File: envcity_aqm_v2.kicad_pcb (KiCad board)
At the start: 2 copper layers, 100 x 100 mm, 133 parts, among them IC1 DS1307ZN+, IC2 DMMT5401-7F, IC3 DMMT5401-7F, IC4 DMMT5401-7-F, IC6 ESP32-S2-SOLO-N4R2, J1 USB_B_Micro, J12 Conn_01x06_Male, J13 Conn_01x06_Male, J14 Conn_01x08_Pin, J15 Conn_01x02_Male, J16 Conn_01x02_Male, J2 Screw_Terminal_01x02, J3 Screw_Terminal_01x02, J4 Micro_SD_Card, J5 Conn_01x03_Male, J6 Conn_01x04_Male, J7 Conn_01x06_Pin, Q1 DMG2301L / DMP2045U, Q2 DMG2301L / DMP2045U, Q3 DMG2301L, Q4 DMG2301L, Q5 DMG2301L / DMP2045U, Q6 DMG2301L, Q7 DMN10H220L, Q8 DMN10H220L, SW1 RESET, SW2 BOOT, U1 TP4056, U10 RFM95W-915S2, U11 ADS1115IDGS, U2 USBLC6-2SC6, U3 MT3608, U4 MT3608, U5 LM2596S-5, U6 AP2112K-3.3, U7 DHT11, U8 AP2112K-3.3, U9 74HC4067DB, Y2 AB26TRB

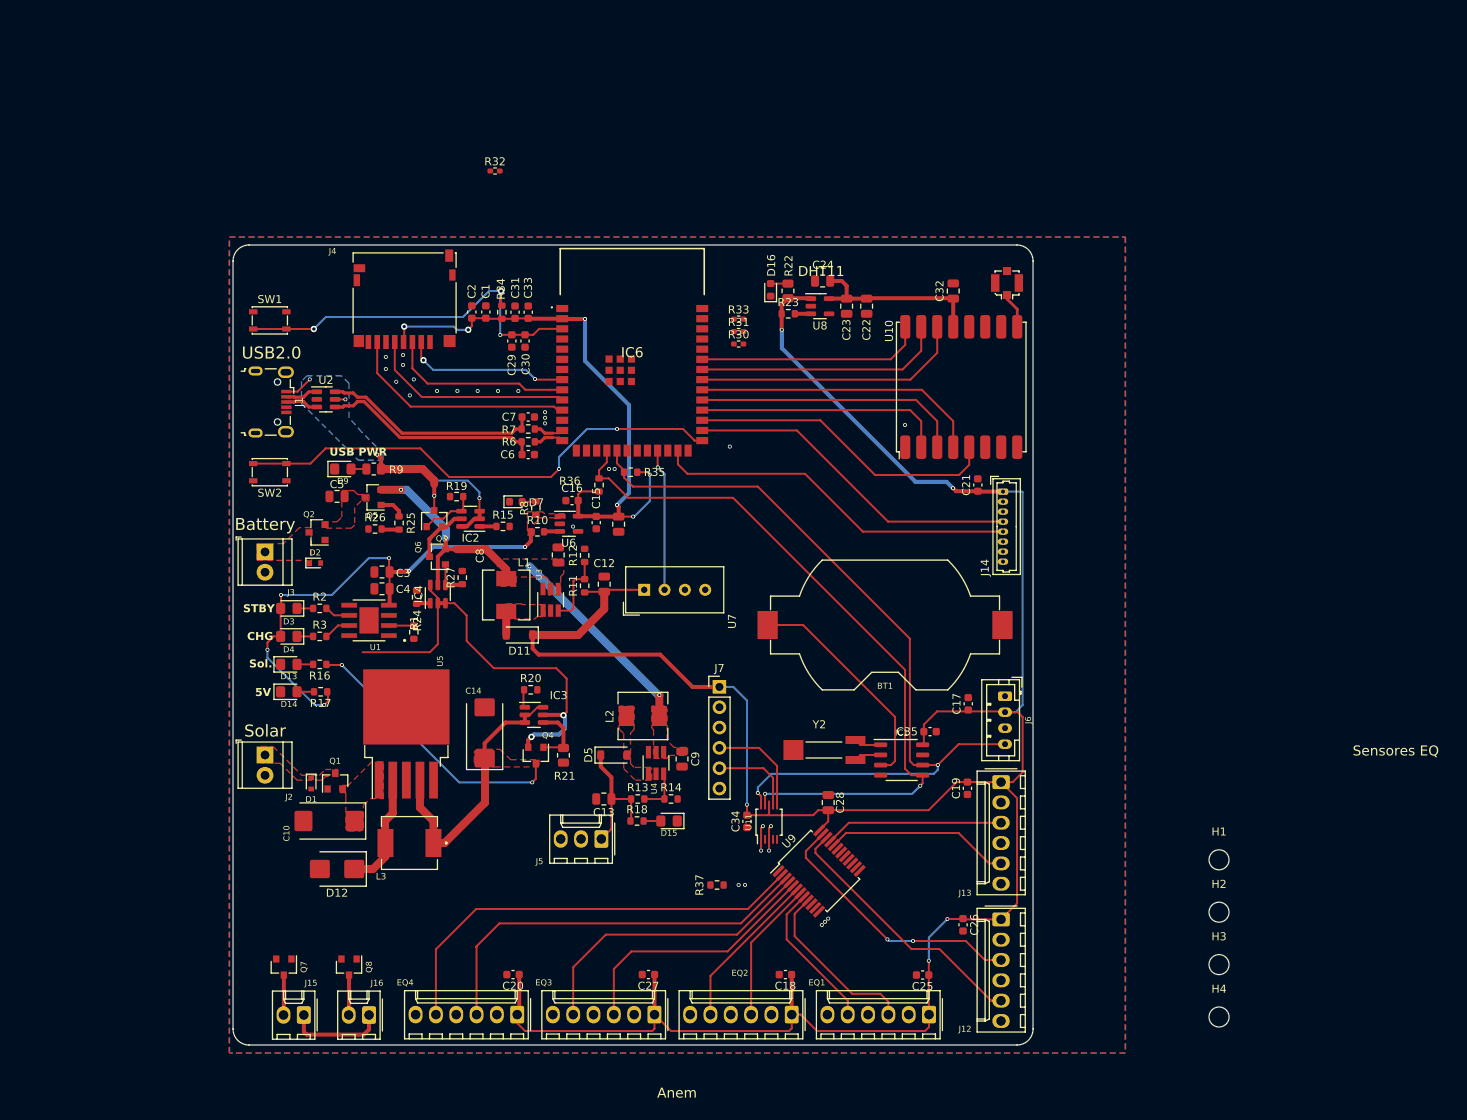
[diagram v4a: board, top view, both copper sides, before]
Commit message: Trocando o modelo do cartaoSD
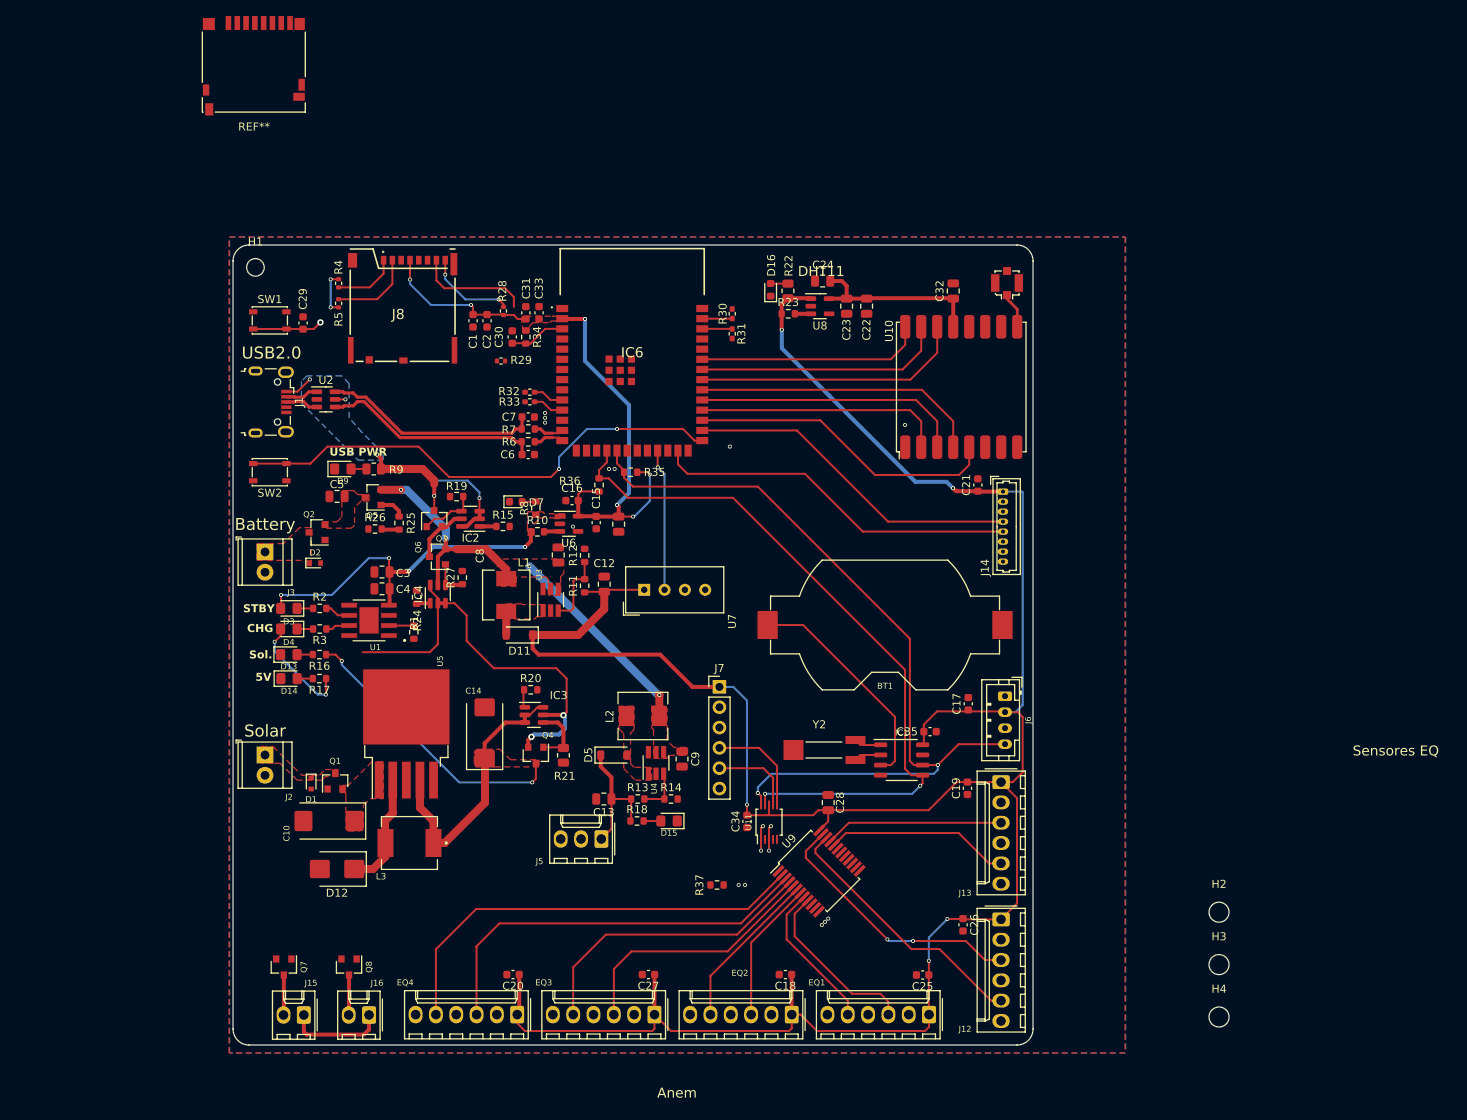
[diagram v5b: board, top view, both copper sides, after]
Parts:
- removed J4: Micro_SD_Card, Connector_Card:microSD_HC_Hirose_DM3D-SF
- added J8: 503398-1892, Molex 503398-1892:503398-1892, F.Cu at (125.7, 60.5)
- added R28: 10k, Resistor_SMD:R_0402_1005Metric, F.Cu at (144.8, 68.2)
- added R29: 10k, Resistor_SMD:R_0402_1005Metric, F.Cu at (144.5, 74.5)
- added R4: 10k, Resistor_SMD:R_0402_1005Metric, F.Cu at (124.2, 64.8)
- added R5: 10k, Resistor_SMD:R_0402_1005Metric, F.Cu at (124.2, 67.3)
- added REF**: microSD_HC_Hirose_DM3D-SF, Connector_Card:microSD_HC_Hirose_DM3D-SF, F.Cu at (113.6, 37.6)
- H1: footprint MountingHole:MountingHole_2.5mm -> MountingHole:MountingHole_2.2mm_M2
- moved H1 141.4 mm to (113.8, 62.8)
- moved R33 28.1 mm to (148.1, 79.6), turned to 180 degrees
- moved R32 28.0 mm to (148.1, 78.4), turned to 180 degrees
- moved C29 26.2 mm to (119.8, 69.8), turned to 90 degrees
- moved R34 4.31 mm to (147.6, 71.5), turned to -90 degrees
- moved R30 3.86 mm to (173.4, 68.6), turned to 90 degrees
- moved C2 2.20 mm to (142.8, 69.5), turned to -90 degrees
- moved C1 1.94 mm to (141.0, 69.5), turned to -90 degrees
- moved C30 1.68 mm to (145.9, 71.5), turned to 90 degrees
- moved R17 1.66 mm to (121.8, 114.2)
- moved D14 1.65 mm to (118.0, 114.2)
- moved C31 1.35 mm to (147.6, 68.5)
- moved C33 1.35 mm to (149.2, 68.5)
- moved R16 1.23 mm to (121.8, 111.2)
- moved D13 1.22 mm to (118.0, 111.2)
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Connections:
- IC6 pad 10: /SD_SCK -> /S2
- IC6 pad 11: /SD_MISO -> /S3
- IC6 pad 38: /IO2 -> /S1
- IC6 pad 39: /IO1 -> /S0
- IC6 pad 4: /S0 -> unconnected-(IC6-IO4-Pad4)
- IC6 pad 5: /S1 -> /SD_CS
- IC6 pad 6: /S2 -> /SD_MOSI
- IC6 pad 7: /S3 -> /SD_SCK
- IC6 pad 8: /SD_CS -> /SD_MISO
- IC6 pad 9: /SD_MOSI -> unconnected-(IC6-IO16-Pad9)
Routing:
- net /EN: track 48.4 -> 15.8 mm, vias 3 -> 1
- net /SD_SCK: track 26.0 -> 0.00 mm
- net /SD_MOSI: track 23.1 -> 0.07 mm
- net /SD_MISO: track 28.9 -> 14.3 mm
- net /DAT1: track 0.00 -> 11.3 mm, vias 0 -> 2
- net /SD_CS: track 20.7 -> 10.5 mm, vias 2 -> 0
- net /DAT2: track 0.00 -> 8.01 mm
- net +5V: track 395.0 -> 390.0 mm
- net /S3: track 0.00 -> 3.88 mm
- net /S2: track 0.00 -> 3.85 mm
- net /S1: track 0.00 -> 3.76 mm
- net /S0: track 0.00 -> 3.76 mm
- net +3V3: track 73.9 -> 76.2 mm, vias 6 -> 8
- net Vsolar_reg: track 68.9 -> 69.5 mm
- net GND: vias 29 -> 17
- added copper zone on F.Cu, net +3V3

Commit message: running DRC and fixing some errors
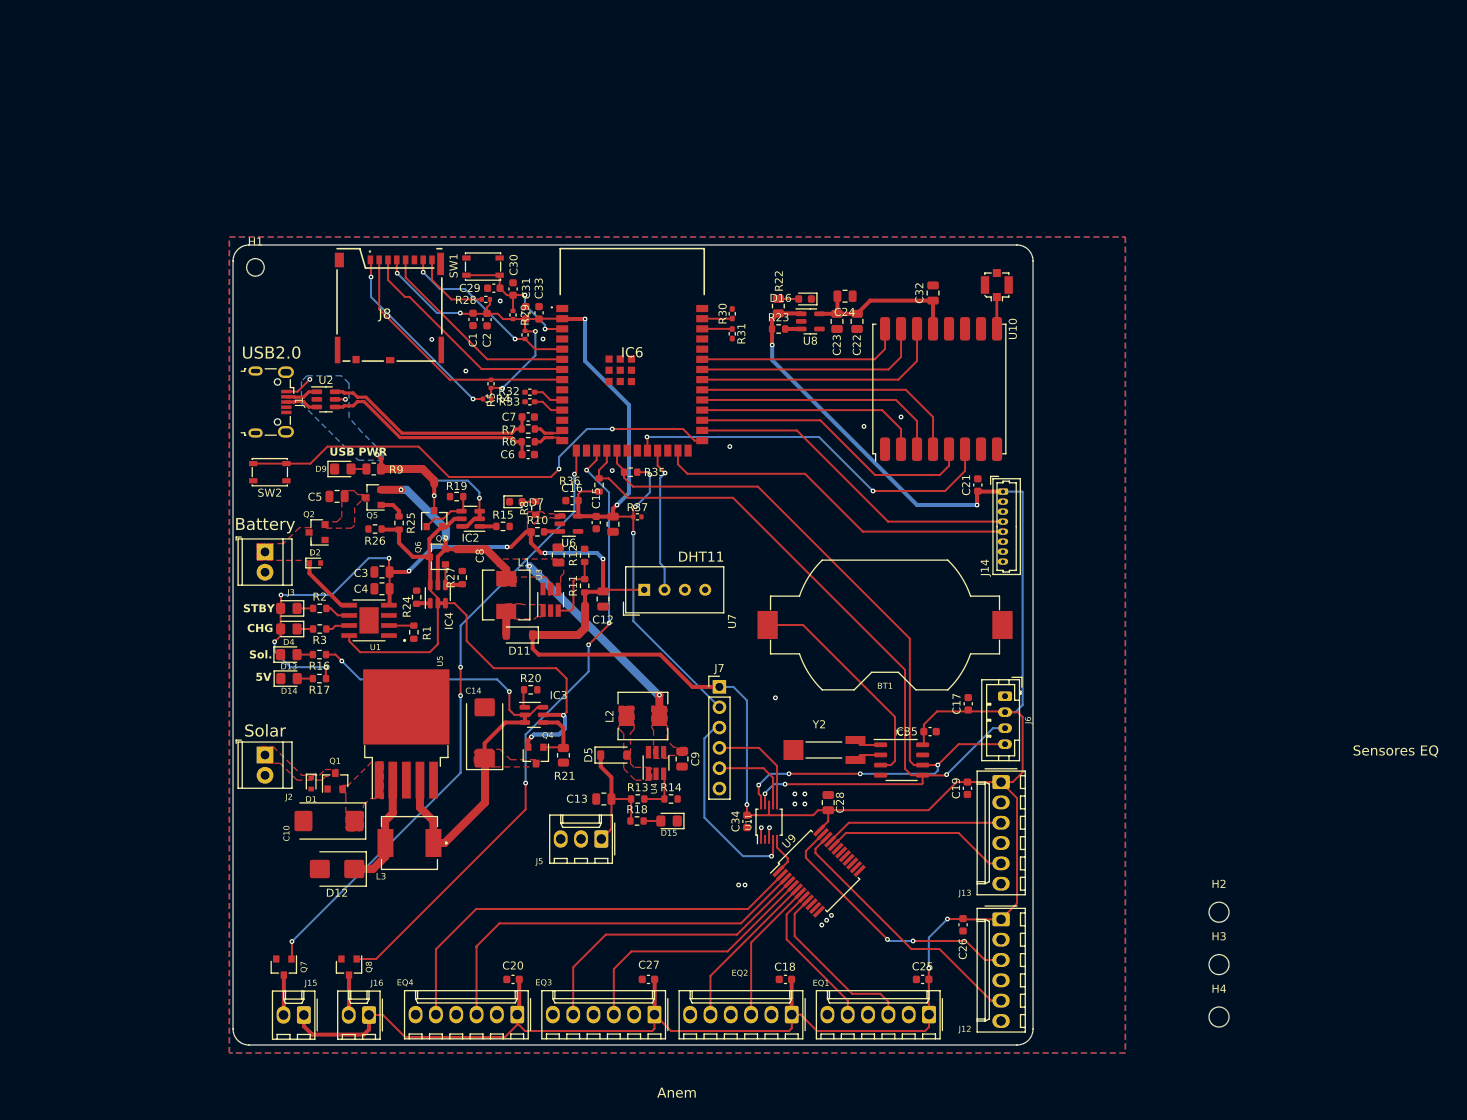
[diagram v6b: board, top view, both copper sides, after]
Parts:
- removed REF**: microSD_HC_Hirose_DM3D-SF, Connector_Card:microSD_HC_Hirose_DM3D-SF
- R34, R37: footprint Resistor_SMD:R_0603_1608Metric -> Resistor_SMD:R_0402_1005Metric
- moved R37 47.1 mm to (161.5, 94.0)
- moved SW1 27.5 mm to (142.2, 62.7)
- moved C29 24.2 mm to (143.6, 65.4), turned to 180 degrees
- moved R4 23.5 mm to (142.8, 79.2), turned to 180 degrees
- moved R5 21.5 mm to (143.2, 77.3)
- moved C30 6.00 mm to (146.0, 65.5)
- moved D16 4.45 mm to (182.5, 66.8), turned to 180 degrees
- moved R29 4.43 mm to (147.5, 71.2), turned to -90 degrees
- moved C24 3.38 mm to (187.5, 66.4), turned to 0 degrees
- moved R34 3.18 mm to (146.0, 68.8), turned to 90 degrees
- moved R28 2.63 mm to (142.6, 66.8), turned to 180 degrees
- moved C32 2.54 mm to (198.5, 66.0)
- moved U10 2.54 mm to (199.5, 78.0)
- moved R22 2.25 mm to (179.2, 67.6)
- moved R23 2.25 mm to (179.2, 70.5)
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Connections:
- IC6 pad 24: /IO33 -> /ADS_ALERT
- IC6 pad 5: /SD_CS -> /SD_MISO
- IC6 pad 6: /SD_MOSI -> /SD_SCK
- IC6 pad 7: /SD_SCK -> /SD_MOSI
- IC6 pad 8: /SD_MISO -> /SD_CS
- J7 pad 3: /AIN1 -> /AIN0
- U9 pad 1: /AIN0 -> /AIN1
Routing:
- net /FAN2: track 0.00 -> 79.7 mm, vias 0 -> 4
- net /FAN1: track 0.00 -> 78.3 mm, vias 0 -> 4
- net /RFM_RST: track 0.00 -> 48.0 mm, vias 0 -> 2
- net +3V3: track 76.2 -> 120.3 mm, vias 8 -> 9
- net +5V: track 390.0 -> 425.8 mm, vias 11 -> 13
- net /SD_MOSI: track 0.07 -> 28.9 mm
- net /SD_SCK: track 0.00 -> 26.0 mm
- net /AIN0: track 0.00 -> 24.9 mm, vias 0 -> 1
- net /SD_CS: track 10.5 -> 32.8 mm
- net /DAT2: track 8.01 -> 23.9 mm, vias 0 -> 2
- net /SDA: track 89.6 -> 102.4 mm, vias 2 -> 3
- net Vexternal: track 64.2 -> 76.9 mm
- net /SD_MISO: track 14.3 -> 22.9 mm, vias 0 -> 2
- net Vbat: track 0.00 -> 7.92 mm
- net Vsolar_reg: track 69.5 -> 63.6 mm
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- removed copper zone on F.Cu, net +3V3
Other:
- rule pad_to_mask_clearance: 0.051 -> 0.038
- rule solder_mask_min_width: 0.25 -> 0.1

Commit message: Corrigindo LCSC part #
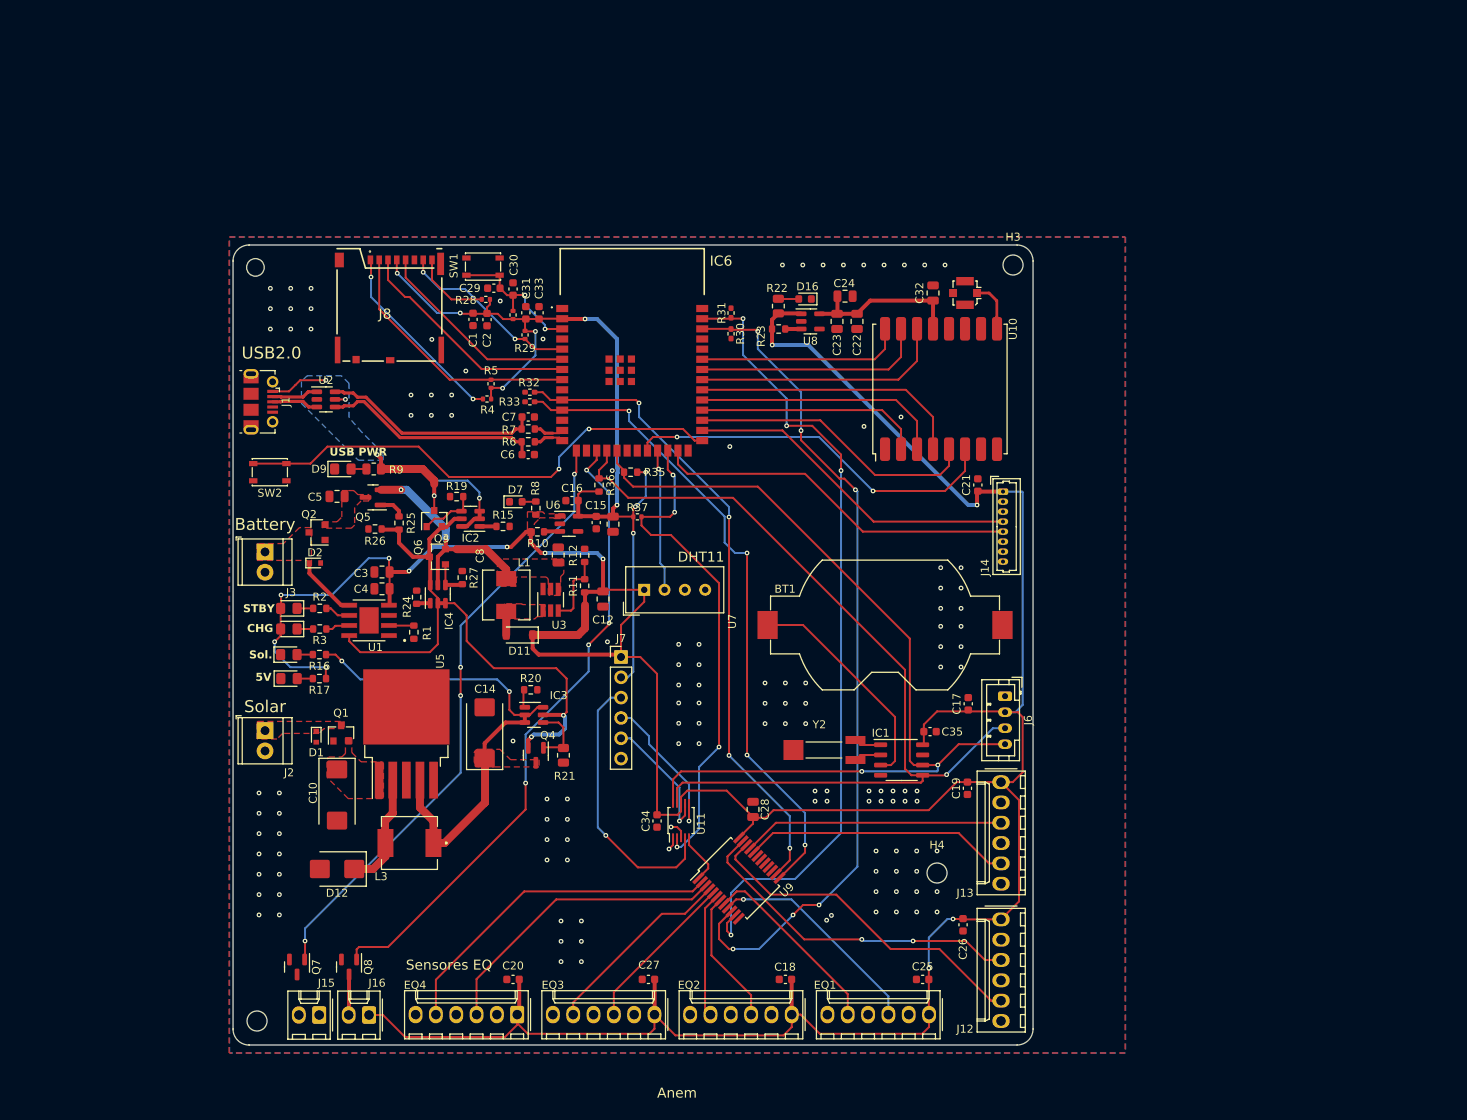
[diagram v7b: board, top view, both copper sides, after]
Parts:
- removed C13, C9: 22uF-X5R, Capacitor_SMD:C_0805_2012Metric
- removed D15: LED, LED_SMD:LED_0805_2012Metric_Pad1.15x1.40mm_HandSolder
- removed D5: BAT54W, Diode_SMD:D_SOD-123
- removed J5: Conn_01x03_Male, Connector_Molex:Molex_KK-254_AE-6410-03A_1x03_P2.54mm_Vertical
- removed L2: XR0530-100M, Inductor_SMD:L_Chilisin_BMRA00050530
- removed R13: 30K, Resistor_SMD:R_0603_1608Metric
- removed R14: 2.2K, Resistor_SMD:R_0603_1608Metric
- removed R18: 9K1, Resistor_SMD:R_0603_1608Metric
- removed U4: MT3608, Package_TO_SOT_SMD:SOT-23-6_Handsoldering
- C14: value 220uF-Tantalum -> 220uF-
- J1: footprint Connector_USB:USB_Micro-B_Wuerth_629105150521 -> Connector_USB:USB_Micro-B_Molex-105017-0001
- moved H2 121.0 mm to (114.0, 157.0)
- moved H3 91.2 mm to (208.5, 62.5)
- moved H4 39.6 mm to (199.0, 138.5)
- moved J7 12.9 mm to (159.5, 111.5)
- moved C34 11.2 mm to (164.0, 132.0)
- moved U11 11.0 mm to (167.0, 131.9)
- moved U9 10.1 mm to (174.2, 139.1)
- moved C28 9.44 mm to (176.0, 130.6)
- moved Q1 6.04 mm to (124.5, 121.0)
- moved D1 5.88 mm to (121.4, 121.5)
- moved AE1 4.10 mm to (202.5, 66.0), turned to 90 degrees
- moved C10 3.40 mm to (124.0, 128.8), turned to -90 degrees
- moved J2 3.05 mm to (115.0, 120.7)
- moved R31 2.60 mm to (173.2, 68.5), turned to 90 degrees
- moved R30 2.50 mm to (173.2, 71.1), turned to -90 degrees
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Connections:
- IC6 pad 38: /S1 -> /S0
- IC6 pad 39: /S0 -> /S1
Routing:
- net /S0: track 3.76 -> 105.4 mm, vias 0 -> 6
- net /S1: track 3.76 -> 101.6 mm, vias 0 -> 4
- net /S3: track 3.88 -> 82.0 mm, vias 0 -> 4
- net /S2: track 3.85 -> 81.1 mm, vias 0 -> 4
- net /ADS_ALERT: track 0.00 -> 62.8 mm, vias 0 -> 4
- net Vsys: track 52.9 -> 27.3 mm, vias 4 -> 2
- net +9V: track 16.8 -> 0.00 mm
- net /I5: track 37.4 -> 24.4 mm
- net /I6: track 50.7 -> 37.9 mm
- net /I7: track 55.3 -> 42.7 mm
- net /I4: track 32.4 -> 20.3 mm
- net /SDA: track 102.4 -> 113.4 mm, vias 3 -> 1
- net /SCL: track 102.7 -> 113.3 mm, vias 4 -> 2
- net /I11: track 23.1 -> 33.5 mm
- net /I10: track 22.3 -> 32.7 mm
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- removed copper zone on F.Cu, net /BST_SW_9V
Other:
- rule pad_to_mask_clearance: 0.038 -> 0
